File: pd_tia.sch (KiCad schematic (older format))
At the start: 11 parts, among them U1 ED2610, U2 LM2940

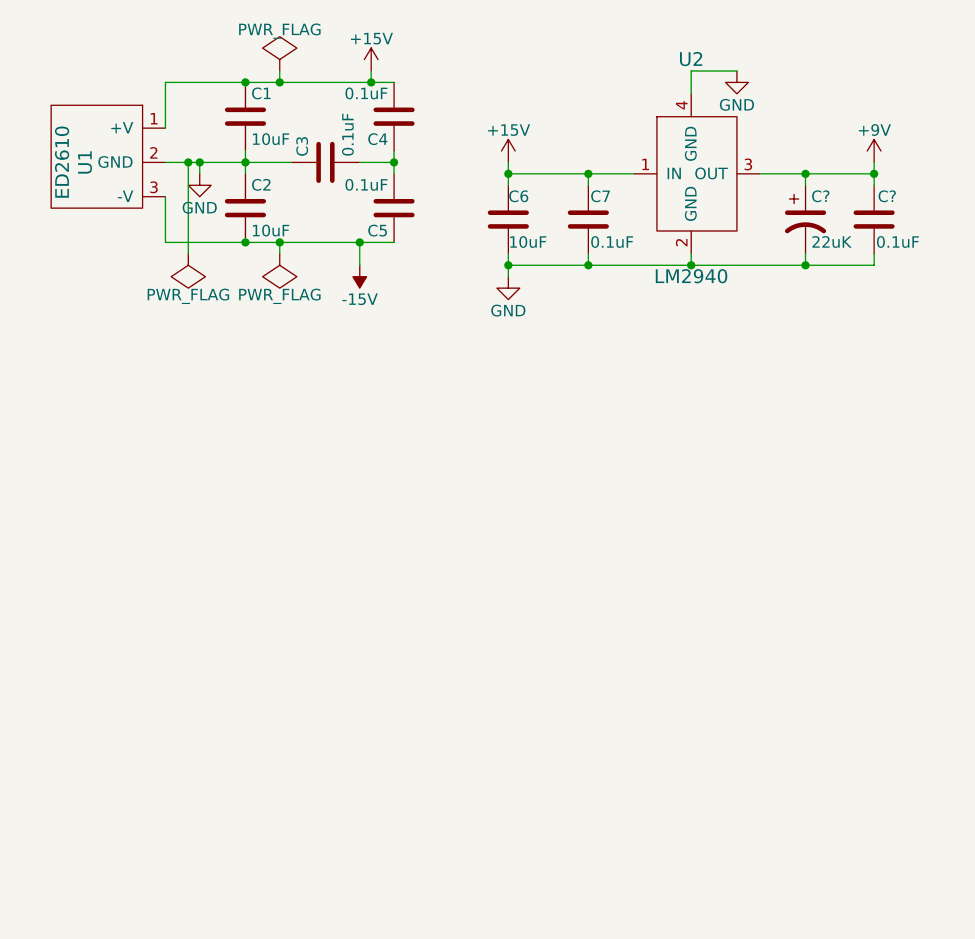
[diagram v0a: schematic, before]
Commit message: Schematic done
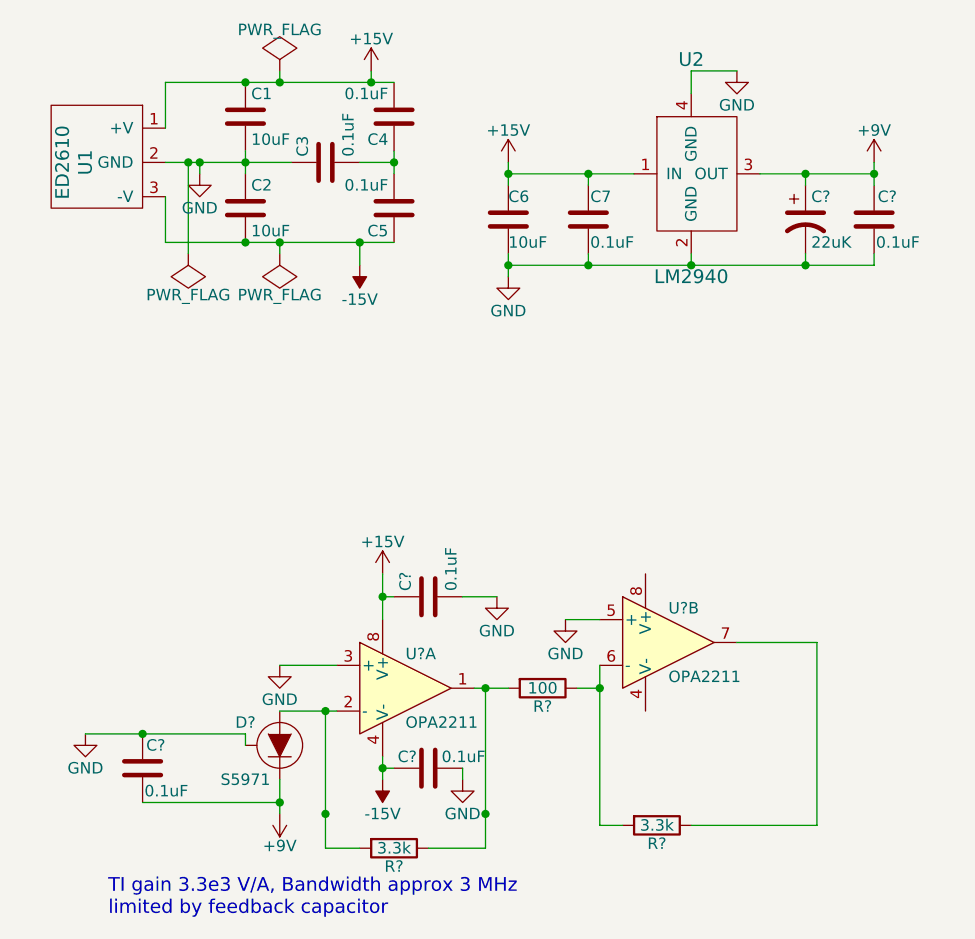
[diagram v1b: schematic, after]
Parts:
- added C? (x3): 0.1uF, Capacitors_SMD:C_0805_HandSoldering, symbol C
- added D?: S5971, TO_SOT_Packages_THT:TO-18-3, symbol S5971
- added R? (x2): 3.3k, Resistors_SMD:R_0805_HandSoldering, symbol R
- added R?: 100, Resistors_SMD:R_0805_HandSoldering, symbol R
- added U? (x2): OPA2211, symbol OPA2211
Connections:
- net +15V: now also C?.1, U?.8 (V+)
- net +9V: now also C?.1, D?.1 (K)
- net -15V: now also C?.1, U?.4 (V-)
- net GND: now also C?.2, C?.2, C?.2, D?.2 (Case), U?.3 (+), U?.5 (+)
- new net: D?.3 (A), R?.2, U?.2 (-)
- new net: R?.1, R?.2, U?.1
- new net: R?.1, R?.2, U?.6 (-)
- new net: R?.1, U?.7
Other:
- note added: "TI gain 3.3e3 V/A, Bandwidth approx 3 MHz\nlimited by feedback capacitor"

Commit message: Autorouter found a solution, but on a bigger board
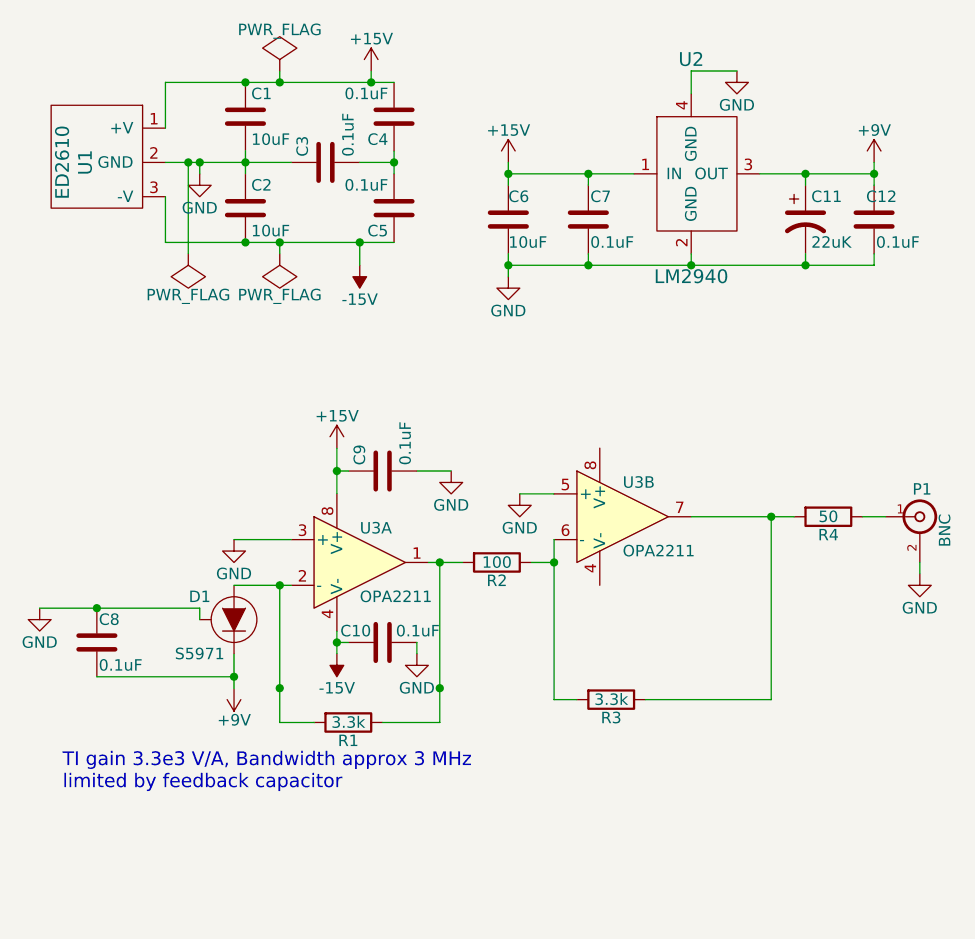
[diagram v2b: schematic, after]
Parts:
- added P1: BNC, footprints:BNC_Isolated_31-5431-10RFX, symbol BNC
- added R4: 50, Resistors_SMD:R_0805_HandSoldering, symbol R
- U1: footprint (none) -> footprints:ED2610
- U3: renamed from U?; footprint (none) -> Housings_SOIC:SOIC-8-1EP_3.9x4.9mm_Pitch1.27mm
- gave numbers to parts that had none: 9
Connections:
- net GND: now also P1.2 (Ext)
- net at R3.1, U3.7: now also R4.2
- new net: P1.1 (In), R4.1
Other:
- moved on the sheet: C10, C8, C9, D1, R1, R2, R3, U3A, U3B

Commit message: Changed BNC footprint
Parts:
- P1: footprint footprints:BNC_Isolated_31-5431-10RFX -> footprints:Dual-BNC-ARF2136
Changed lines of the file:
@@
 F 0 "P1" H 5160 3270 50  0000 C CNN
 F 1 "BNC" V 5260 3090 50  0000 C CNN
-F 2 "footprints:BNC_Isolated_31-5431-10RFX" H 5150 3150 50  0001 C CNN
+F 2 "footprints:Dual-BNC-ARF2136" H 5150 3150 50  0001 C CNN
 F 3 "" H 5150 3150 50  0000 C CNN
 	1    5150 3150

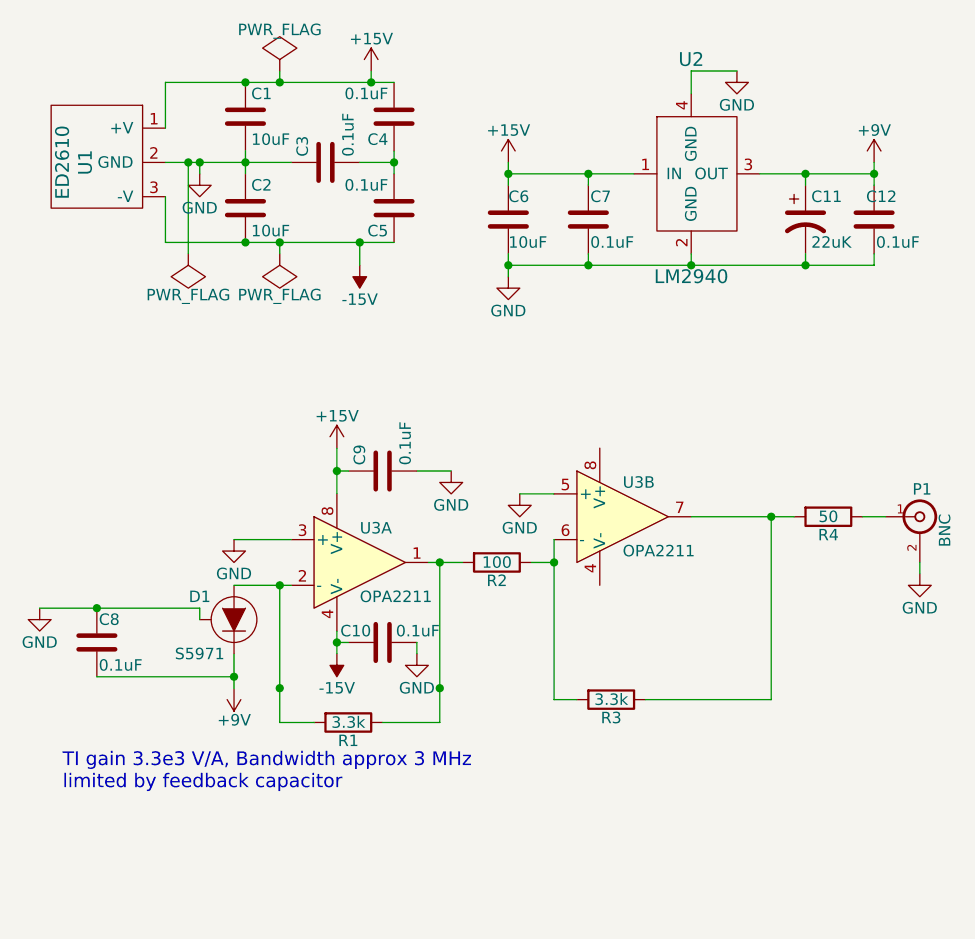
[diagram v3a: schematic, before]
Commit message: First shot at layout... almost all components in
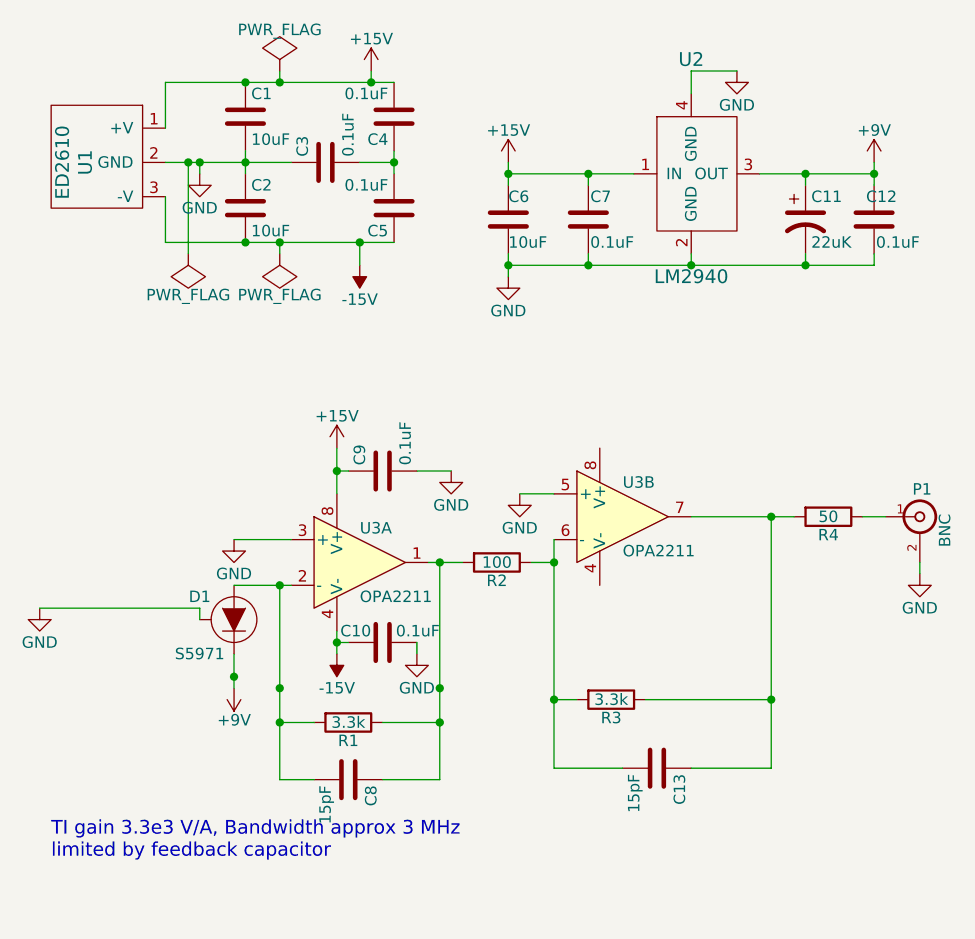
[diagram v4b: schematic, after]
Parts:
- added C13: 15pF, Capacitors_SMD:C_0603_HandSoldering, symbol C
- C8: value 0.1uF -> 15pF; footprint Capacitors_SMD:C_0805_HandSoldering -> Capacitors_SMD:C_0603_HandSoldering
- P1: footprint footprints:Dual-BNC-ARF2136 -> footprints:SMA_throughhole
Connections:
- net +9V: no longer C8.1
- net GND: no longer C8.2
- net at D1.3 (A), R1.2, U3.2 (-): now also C8.2
- net at R1.1, R2.2, U3.1: now also C8.1
- net at R2.1, R3.2, U3.6 (-): now also C13.2
- net at R3.1, R4.2, U3.7: now also C13.1
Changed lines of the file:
@@
 LIBS:valves
 LIBS:all_components
+LIBS:pd_tia-cache
 EELAYER 25 0
 EELAYER END
@@
 	-1   0    0    1
 $EndComp
-$Comp
-L C C8
-U 1 1 58C05EA3
-P 1550 3700
-F 0 "C8" H 1450 3600 50  0000 L CNN
-F 1 "0.1uF" H 1350 3800 50  0000 L CNN
-F 2 "Capacitors_SMD:C_0805_HandSoldering" H 1588 3550 50  0001 C CNN
-F 3 "" H 1550 3700 50  0000 C CNN
-	1    1550 3700
-	-1   0    0    1
-$EndComp
 Wire Wire Line
 	1850 1250 2850 1250
@@
 Wire Wire Line
 	2150 3750 2150 3900
-Wire Wire Line
-	1550 3850 2150 3850
 Connection ~ 2150 3850
 Wire Wire Line
@@
 	1    0    0    -1
 $EndComp
-Connection ~ 1550 3550
 $Comp
 L OPA2211 U3
@@
 $EndComp
 Wire Wire Line
-	2350 3450 2350 4050
+	2350 3450 2350 4300
 Connection ~ 2350 3450
 Wire Wire Line
-	3050 3350 3050 4050
+	3050 3350 3050 4300
 Wire Wire Line
 	3000 3350 3150 3350
@@
 $EndComp
 Wire Wire Line
-	3550 3250 3550 3950
+	3550 3250 3550 4250
 Wire Wire Line
 	3550 3950 3650 3950
@@
 	3950 3950 4500 3950
 Wire Wire Line
-	4500 3950 4500 3150
+	4500 3150 4500 4250
 Wire Wire Line
 	4150 3150 4600 3150
@@
 	3450 3350 3550 3350
 Connection ~ 3550 3350
-Text Notes 1400 4350 0    60   ~ 0
+Text Notes 1350 4650 0    60   ~ 0
 TI gain 3.3e3 V/A, Bandwidth approx 3 MHz\nlimited by feedback capacitor
 $Comp
@@
 F 0 "P1" H 5160 3270 50  0000 C CNN
 F 1 "BNC" V 5260 3090 50  0000 C CNN
-F 2 "footprints:Dual-BNC-ARF2136" H 5150 3150 50  0001 C CNN
+F 2 "footprints:SMA_throughhole" H 5150 3150 50  0001 C CNN
 F 3 "" H 5150 3150 50  0000 C CNN
 	1    5150 3150
@@
 Wire Wire Line
 	5150 3350 5150 3400
+$Comp
+L C C8
+U 1 1 58C6AC99
+P 2650 4300
+F 0 "C8" H 2675 4400 50  0000 L CNN
+F 1 "15pF" H 2675 4200 50  0000 L CNN
+F 2 "Capacitors_SMD:C_0603_HandSoldering" H 2688 4150 50  0001 C CNN
+F 3 "" H 2650 4300 50  0000 C CNN
+	1    2650 4300
+	0    1    1    0
+$EndComp
+$Comp
+L C C13
+U 1 1 58C6AD21
+P 4000 4250
+F 0 "C13" H 4025 4350 50  0000 L CNN
+F 1 "15pF" H 4025 4150 50  0000 L CNN
+F 2 "Capacitors_SMD:C_0603_HandSoldering" H 4038 4100 50  0001 C CNN
+F 3 "" H 4000 4250 50  0000 C CNN
+	1    4000 4250
+	0    1    1    0
+$EndComp
+Wire Wire Line
+	3550 4250 3850 4250
+Connection ~ 3550 3950
+Wire Wire Line
+	4500 4250 4150 4250
+Connection ~ 4500 3950
+Wire Wire Line
+	2350 4300 2500 4300
+Connection ~ 2350 4050
+Wire Wire Line
+	3050 4300 2800 4300
+Connection ~ 3050 4050
 $EndSCHEMATC

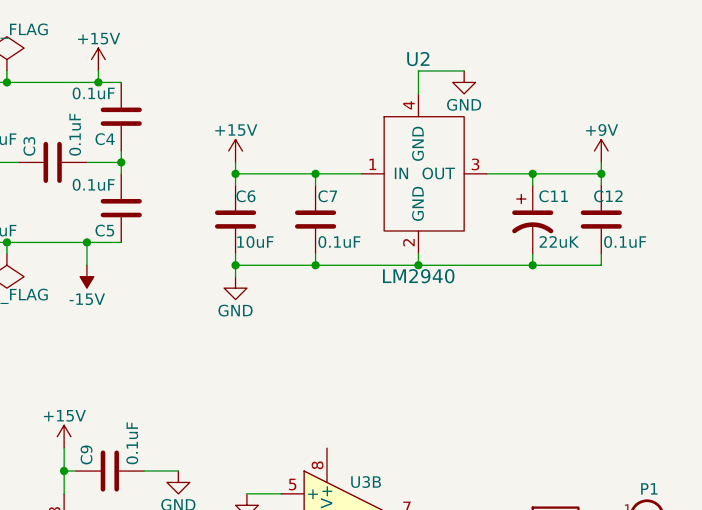
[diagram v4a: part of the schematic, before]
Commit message: More autorouting
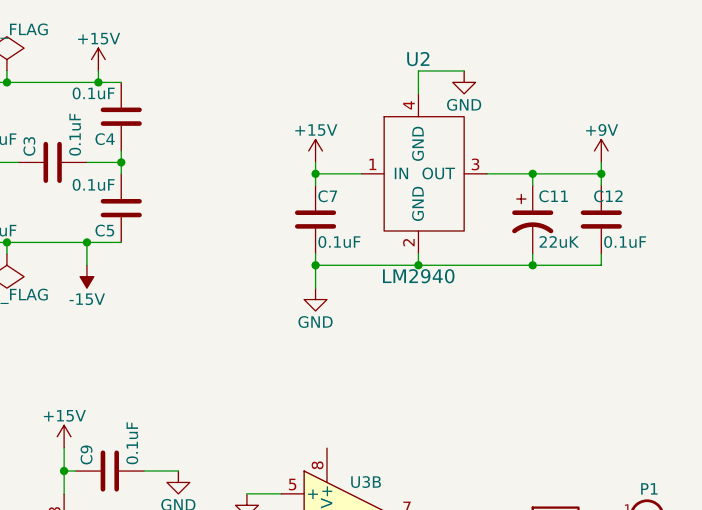
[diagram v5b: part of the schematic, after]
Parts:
- removed C6: 10uF, Capacitors_SMD:C_0805_HandSoldering, symbol C
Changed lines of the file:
@@
 L +15V #PWR06
 U 1 1 58C03C50
-P 3350 1600
-F 0 "#PWR06" H 3350 1450 50  0001 C CNN
-F 1 "+15V" H 3350 1740 50  0000 C CNN
-F 2 "" H 3350 1600 50  0000 C CNN
-F 3 "" H 3350 1600 50  0000 C CNN
-	1    3350 1600
+P 3700 1600
+F 0 "#PWR06" H 3700 1450 50  0001 C CNN
+F 1 "+15V" H 3700 1740 50  0000 C CNN
+F 2 "" H 3700 1600 50  0000 C CNN
+F 3 "" H 3700 1600 50  0000 C CNN
+	1    3700 1600
 	1    0    0    -1
 $EndComp
@@
 $EndComp
 $Comp
-L C C6
-U 1 1 58C03F4F
-P 3350 1850
-F 0 "C6" H 3350 1950 50  0000 L CNN
-F 1 "10uF" H 3350 1750 50  0000 L CNN
-F 2 "Capacitors_SMD:C_0805_HandSoldering" H 3388 1700 50  0001 C CNN
-F 3 "" H 3350 1850 50  0000 C CNN
-	1    3350 1850
-	1    0    0    -1
-$EndComp
-$Comp
 L GND #PWR07
 U 1 1 58C04081
-P 3350 2100
-F 0 "#PWR07" H 3350 1850 50  0001 C CNN
-F 1 "GND" H 3350 1950 50  0000 C CNN
-F 2 "" H 3350 2100 50  0000 C CNN
-F 3 "" H 3350 2100 50  0000 C CNN
-	1    3350 2100
+P 3700 2150
+F 0 "#PWR07" H 3700 1900 50  0001 C CNN
+F 1 "GND" H 3700 2000 50  0000 C CNN
+F 2 "" H 3700 2150 50  0000 C CNN
+F 3 "" H 3700 2150 50  0000 C CNN
+	1    3700 2150
 	1    0    0    -1
 $EndComp
@@
 Connection ~ 2000 1600
 Wire Wire Line
-	3350 1600 3350 1700
-Wire Wire Line
-	3350 2000 3350 2100
-Wire Wire Line
-	3350 2050 4950 2050
-Wire Wire Line
-	3700 2050 3700 2000
-Connection ~ 3350 2050
-Wire Wire Line
-	3350 1650 3900 1650
-Connection ~ 3350 1650
-Wire Wire Line
-	3700 1700 3700 1650
+	3700 2000 3700 2150
+Wire Wire Line
+	3700 1600 3700 1700
 Connection ~ 3700 1650
 Wire Wire Line
@@
 	3050 4300 2800 4300
 Connection ~ 3050 4050
+Wire Wire Line
+	3700 2050 4950 2050
+Wire Wire Line
+	3700 1650 3900 1650
 $EndSCHEMATC
